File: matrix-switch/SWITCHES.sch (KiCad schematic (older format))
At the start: 228 parts, among them J1 Conn_01x02, J10 Conn_01x02, J11 Conn_01x02, J12 Conn_01x02, J13 Conn_01x02, J14 Conn_01x02, J15 Conn_01x02, J16 Conn_01x02, J17 Conn_01x02, J18 Conn_01x02, J19 Conn_01x02, J2 Conn_01x02, J20 Conn_01x02, J21 Conn_01x02, J22 Conn_01x02, J23 Conn_01x02, J24 Conn_01x02, J25 Conn_01x02, J26 Conn_01x02, J27 Conn_01x02, J28 Conn_01x02, J29 Conn_01x02, J3 Conn_01x02, J30 Conn_01x02, J31 Conn_01x02, J32 Conn_01x02, J4 Conn_01x02, J5 Conn_01x02, J6 Conn_01x02, J7 Conn_01x02, J8 Conn_01x02, J9 Conn_01x02, U1 ASSR-1218, U10 ASSR-1218, U100 ASSR-1218, U101 ASSR-1218, U102 ASSR-1218, U103 ASSR-1218, U104 ASSR-1218, U105 ASSR-1218, U106 ASSR-1218, U107 ASSR-1218, U108 ASSR-1218, U109 ASSR-1218, U11 ASSR-1218, U110 ASSR-1218, U111 ASSR-1218, U112 ASSR-1218, U113 ASSR-1218, U114 ASSR-1218, U115 ASSR-1218, U116 ASSR-1218, U117 ASSR-1218, U118 ASSR-1218, U119 ASSR-1218, U12 ASSR-1218, U120 ASSR-1218, U121 ASSR-1218, U122 ASSR-1218, U123 ASSR-1218, U124 ASSR-1218, U125 ASSR-1218, U126 ASSR-1218, U127 ASSR-1218, U128 ASSR-1218, U13 ASSR-1218, U14 ASSR-1218, U15 ASSR-1218, U16 ASSR-1218, U17 ASSR-1218, U18 ASSR-1218, U19 ASSR-1218, U2 ASSR-1218, U20 ASSR-1218, U21 ASSR-1218, U22 ASSR-1218, U23 ASSR-1218, U24 ASSR-1218, U25 ASSR-1218, U26 ASSR-1218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

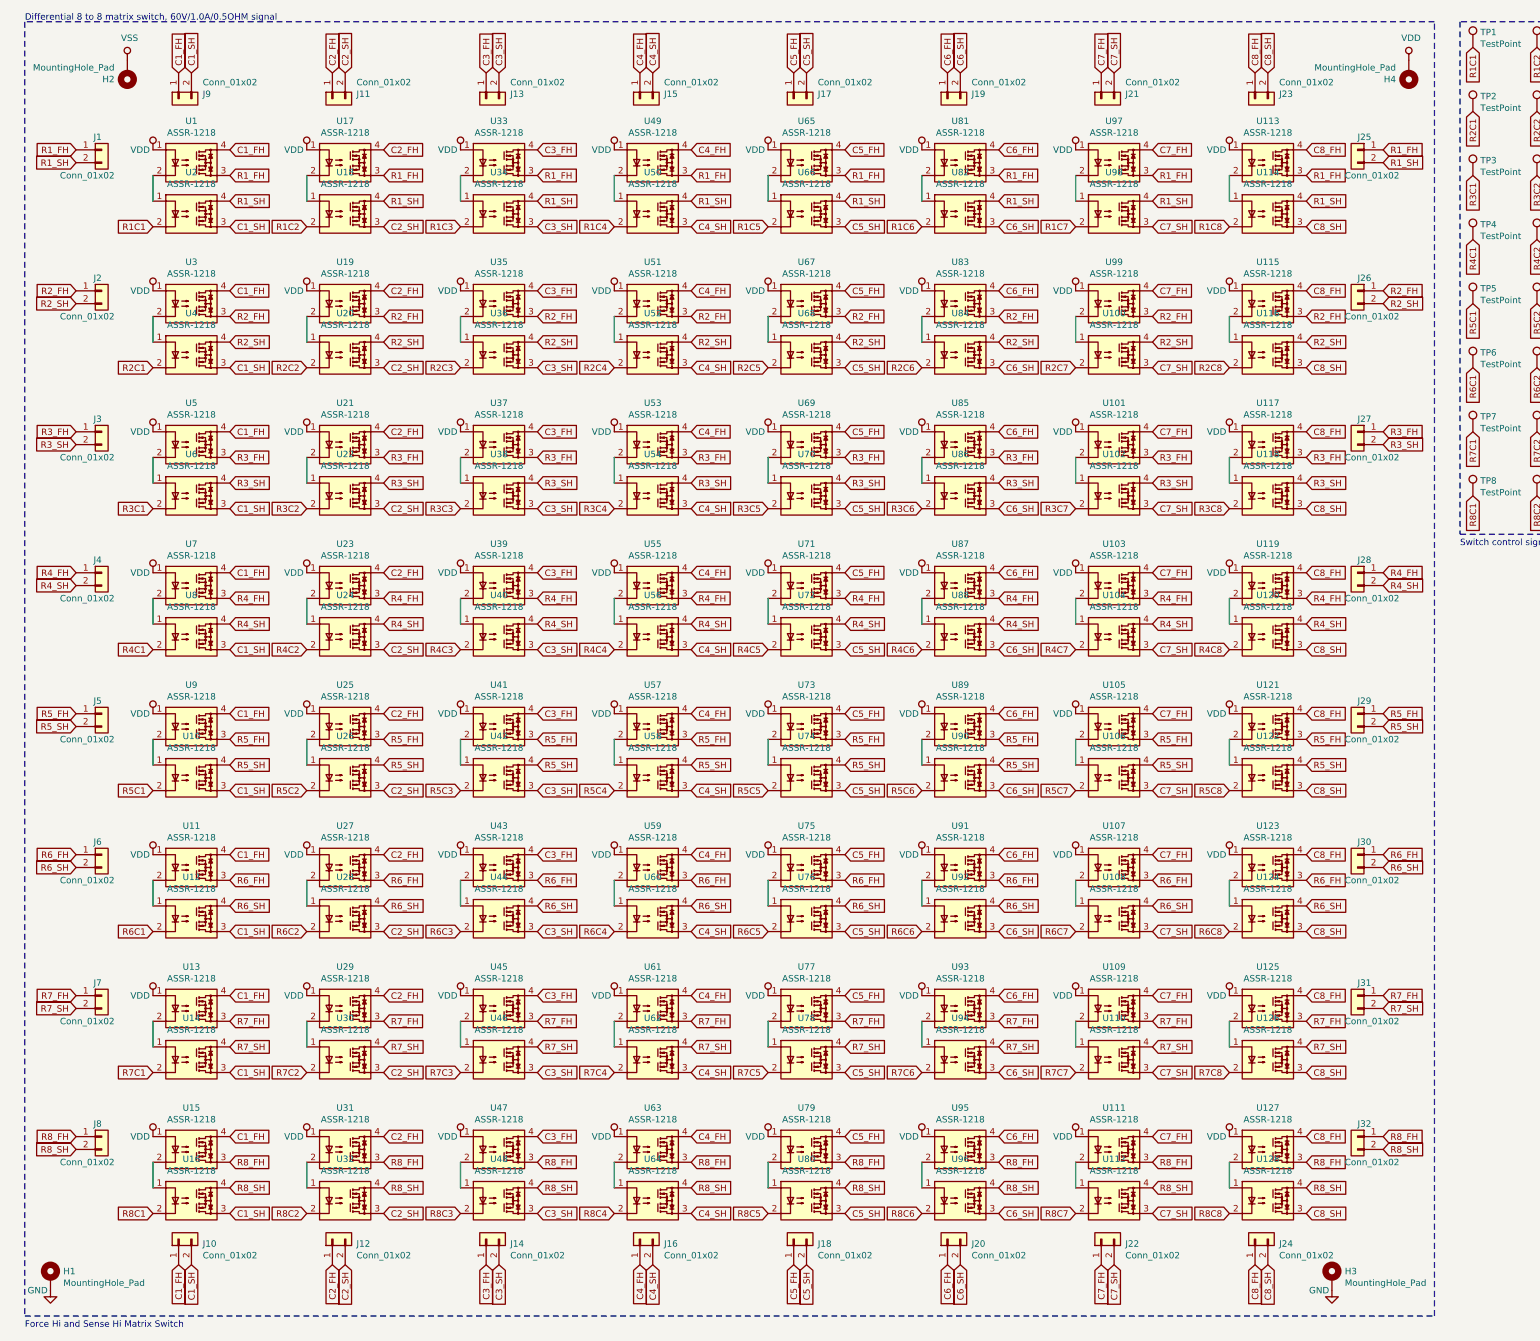
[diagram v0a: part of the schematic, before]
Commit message: wip on matrix switch card edge adapter board
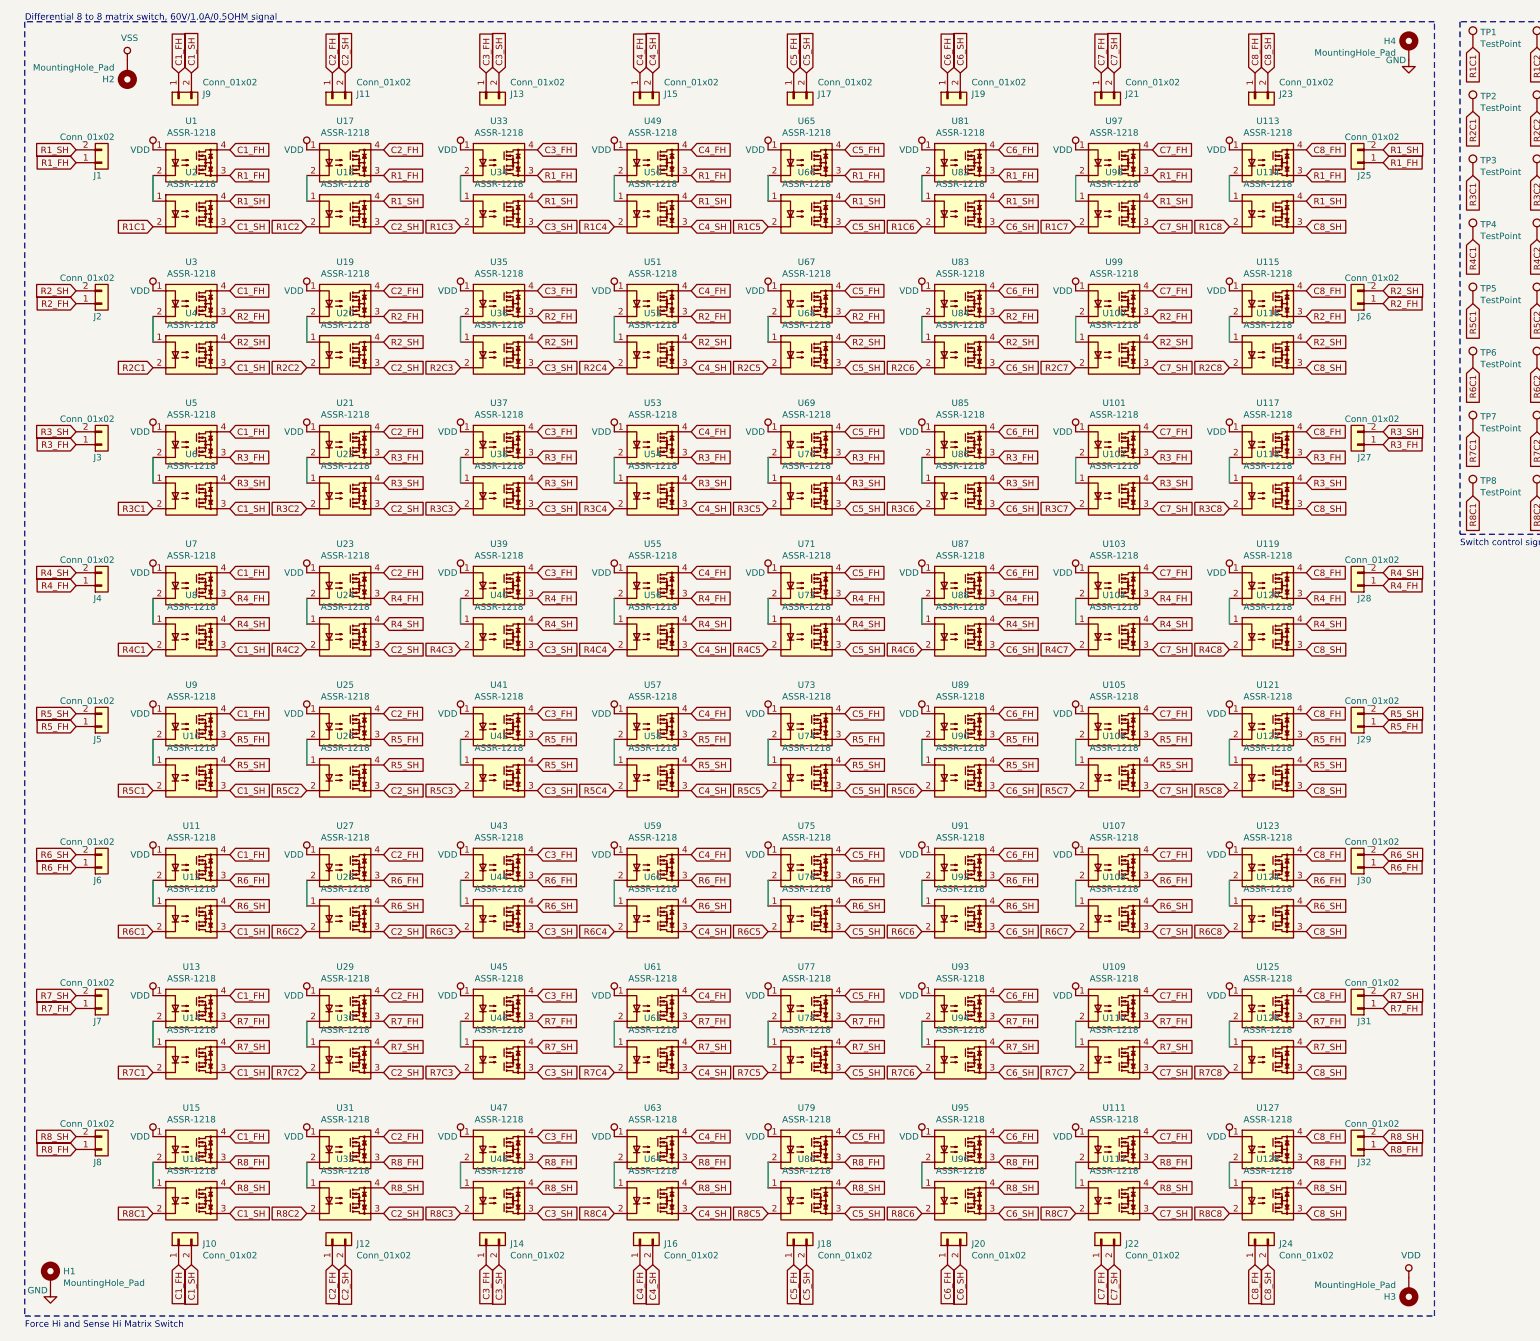
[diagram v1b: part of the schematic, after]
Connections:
- net GND: now also H4.1; no longer H3.1
- net VDD: now also H3.1; no longer H4.1
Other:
- moved on the sheet: H3, H4
